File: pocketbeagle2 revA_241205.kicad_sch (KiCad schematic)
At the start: 1 part, among them U1 PocketBeagle2

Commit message: MDIX routing done
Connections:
- net I2C2_SCL: no longer names the net of U1.28 (I2C2.SCL)
- net I2C2_SDA: no longer names the net of U1.26 (I2C2.SDA)
- no-connect marks 0 -> 39
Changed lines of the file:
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@@
 		(color 0 0 0 0)
 	)
+	(no_connect
+		(at 43.18 62.23)
+	)
+	(no_connect
+		(at 43.18 52.07)
+	)
+	(no_connect
+		(at 91.44 92.71)
+	)
+	(no_connect
+		(at 91.44 115.57)
+	)
+	(no_connect
+		(at 62.23 26.67)
+	)
+	(no_connect
+		(at 82.55 26.67)
+	)
+	(no_connect
+		(at 43.18 92.71)
+	)
+	(no_connect
+		(at 43.18 64.77)
+	)
+	(no_connect
+		(at 95.25 87.63)
+	)
+	(no_connect
+		(at 69.85 138.43)
+	)
+	(no_connect
+		(at 91.44 72.39)
+	)
+	(no_connect
+		(at 91.44 41.91)
+	)
+	(no_connect
+		(at 91.44 85.09)
+	)
+	(no_connect
+		(at 43.18 69.85)
+	)
+	(no_connect
+		(at 43.18 54.61)
+	)
+	(no_connect
+		(at 52.07 26.67)
+	)
+	(no_connect
+		(at 91.44 95.25)
+	)
+	(no_connect
+		(at 80.01 26.67)
+	)
+	(no_connect
+		(at 91.44 59.69)
+	)
+	(no_connect
+		(at 67.31 26.67)
+	)
+	(no_connect
+		(at 43.18 67.31)
+	)
+	(no_connect
+		(at 43.18 36.83)
+	)
+	(no_connect
+		(at 43.18 113.03)
+	)
+	(no_connect
+		(at 91.44 44.45)
+	)
+	(no_connect
+		(at 43.18 72.39)
+	)
+	(no_connect
+		(at 43.18 49.53)
+	)
+	(no_connect
+		(at 91.44 69.85)
+	)
+	(no_connect
+		(at 43.18 59.69)
+	)
+	(no_connect
+		(at 43.18 115.57)
+	)
+	(no_connect
+		(at 43.18 118.11)
+	)
+	(no_connect
+		(at 91.44 36.83)
+	)
+	(no_connect
+		(at 43.18 107.95)
+	)
+	(no_connect
+		(at 43.18 110.49)
+	)
+	(no_connect
+		(at 43.18 130.81)
+	)
+	(no_connect
+		(at 57.15 26.67)
+	)
+	(no_connect
+		(at 43.18 46.99)
+	)
+	(no_connect
+		(at 43.18 125.73)
+	)
+	(no_connect
+		(at 43.18 105.41)
+	)
+	(no_connect
+		(at 91.44 39.37)
+	)
 	(wire
 		(pts
@@
 		(pts
 			(xy 173.99 59.69) (xy 177.8 59.69)
-		)
-		(stroke
-			(width 0)
-			(type default)
-		)
-	)
-	(wire
-		(pts
-			(xy 91.44 85.09) (xy 96.52 85.09)
 		)
 		(stroke
@@
 		)
 	)
-	(global_label "I2C2_SCL"
-		(shape output)
-		(at 96.52 85.09 0)
-		(fields_autoplaced yes)
-		(effects
-			(font
-				(size 1.27 1.27)
-			)
-			(justify left)
-		)
-		(property "Intersheetrefs" "${INTERSHEET_REFS}"
-			(at 108.2742 85.09 0)
-			(effects
-				(font
-					(size 1.27 1.27)
-				)
-				(justify left)
-				(hide yes)
-			)
-		)
-	)
 	(global_label "RGMII_RD0"
 		(shape output)
@@
 				(hide yes)
 			)
-		)
-	)
-	(global_label "I2C2_SDA"
-		(shape bidirectional)
-		(at 95.25 87.63 0)
-		(fields_autoplaced yes)
-		(effects
-			(font
-				(size 1.27 1.27)
-			)
-			(justify left)
-		)
-		(property "Intersheetrefs" "${INTERSHEET_REFS}"
-			(at 108.176 87.63 0)
-			(effects
-				(font
-					(size 1.27 1.27)
-				)
-				(justify left)
-				(hide yes)
-			)

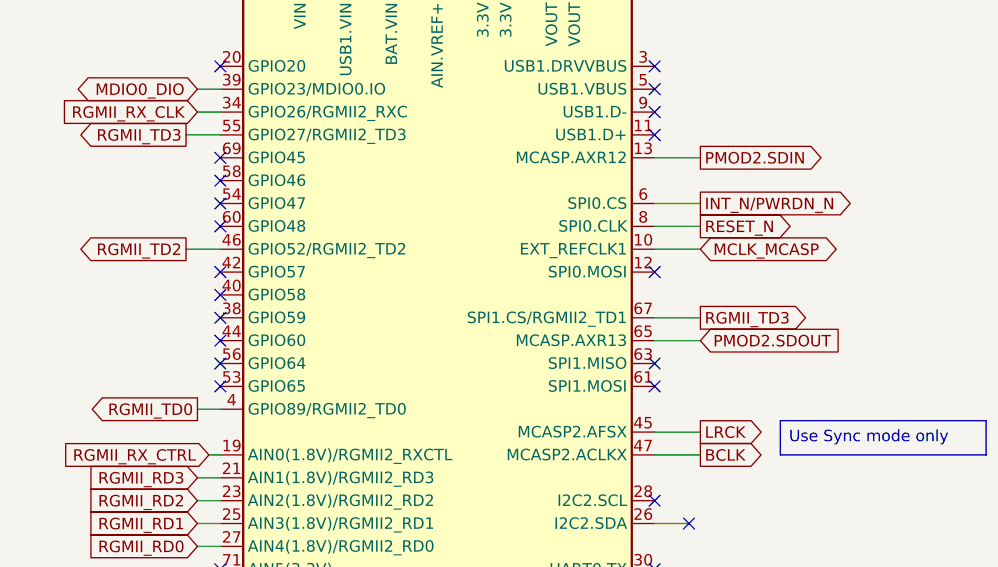
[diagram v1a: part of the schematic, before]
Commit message: Fully routed PCB, missing fligth time matching on the RGMII
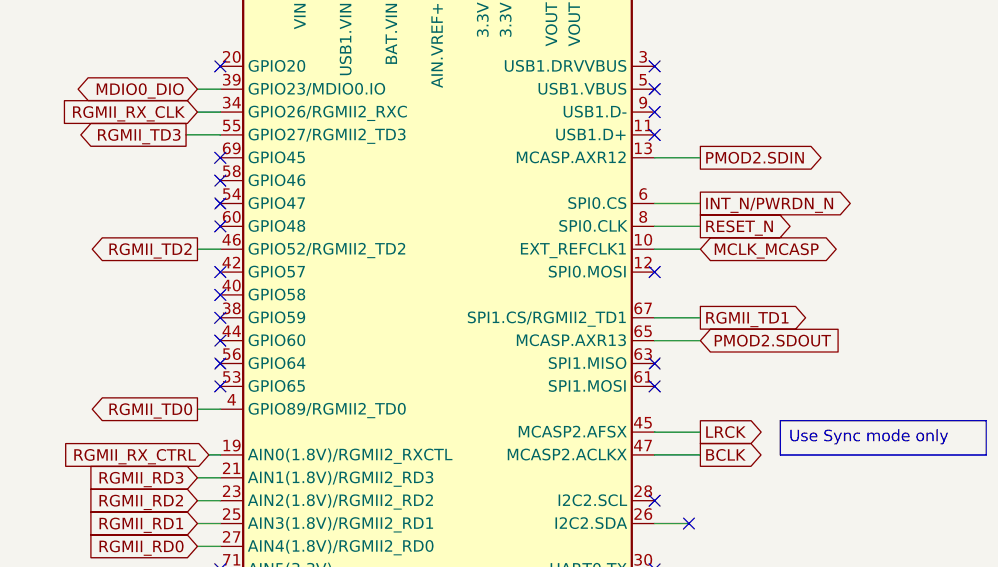
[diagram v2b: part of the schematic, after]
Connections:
- net RGMII_TD1: now also U1.67 (SPI1.CS/RGMII2_TD1)
- net RGMII_TD3: no longer U1.67 (SPI1.CS/RGMII2_TD1)
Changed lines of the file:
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@@
 	(wire
 		(pts
-			(xy 39.37 57.15) (xy 43.18 57.15)
+			(xy 40.64 57.15) (xy 43.18 57.15)
 		)
 		(stroke
@@
 		)
 	)
-	(global_label "RGMII_TD3"
+	(global_label "RGMII_TD1"
 		(shape output)
 		(at 96.52 64.77 0)
@@
 	(global_label "RGMII_TD2"
 		(shape output)
-		(at 39.37 57.15 180)
-		(fields_autoplaced yes)
-		(effects
-			(font
-				(size 1.27 1.27)
-			)
-			(justify right)
-		)
-		(property "Intersheetrefs" "${INTERSHEET_REFS}"
-			(at 26.7691 57.15 0)
-			(effects
-				(font
+		(at 40.64 57.15 180)
+		(fields_autoplaced yes)
+		(effects
+			(font
+				(size 1.27 1.27)
+			)
+			(justify right)
+		)
+		(property "Intersheetrefs" "${INTERSHEET_REFS}"
+			(at 28.0391 57.15 0)
+			(effects
+				(font
